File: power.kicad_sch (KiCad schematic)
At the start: 0 parts

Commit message: moved over a lot of schematic from the bitaxe
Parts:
- added C10: 180pF, Capacitor_SMD:C_0805_2012Metric, symbol Device:C
- added C11: 1.5nF, Capacitor_SMD:C_0805_2012Metric, symbol Device:C
- added C12: 0.1uF, Capacitor_SMD:C_0402_1005Metric, symbol Device:C
- added C13: 10uF, Capacitor_SMD:C_0805_2012Metric, symbol Device:C
- added C14: 470pF, Capacitor_SMD:C_0805_2012Metric, symbol Device:C
- added C15: 220uF, TPS40305_supply:CAP_2R5TPE220MAFB, symbol Device:C_Polarized
- added C16: 100uF, Capacitor_SMD:C_1206_3216Metric, symbol Device:C
- added C17: 1uF, Capacitor_SMD:C_0402_1005Metric, symbol Device:C
- added C5, C6, C7: 47uF, Capacitor_SMD:C_1210_3225Metric, symbol Device:C
- added C8: 1uF, Capacitor_SMD:C_0805_2012Metric, symbol Device:C
- added C9: 3.3nF, Capacitor_SMD:C_0402_1005Metric, symbol Device:C
- added L1: 150nH, TPS40305_supply:FP1005R1-R15-R, symbol Device:L
- added Q1, Q2: CSD17311Q5, TPS40305_supply:CSD17311Q5, symbol TPS40305:Q_NMOS_CSD17311Q5
- added R10: 3.32k, Resistor_SMD:R_0402_1005Metric, symbol Device:R_US
- added R11: 80k, Resistor_SMD:R_0402_1005Metric, symbol Device:R_US
- added R12: DNP, Resistor_SMD:R_0402_1005Metric, symbol Device:R_US
- added R5: 3.83k, Resistor_SMD:R_0402_1005Metric, symbol Device:R_US
- added R6: 100k, Resistor_SMD:R_0402_1005Metric, symbol Device:R_US
- added R7: 4.12k, Resistor_SMD:R_0402_1005Metric, symbol Device:R_US
- added R8: 1.33k, Resistor_SMD:R_0402_1005Metric, symbol Device:R_US
- added R9: 4.99k, Resistor_SMD:R_0402_1005Metric, symbol Device:R_US
- added U2: TPS40305, TPS40305_supply:TPS40305, symbol TPS40305:TPS40305
- added U3: DS4432U+, Package_SO:TSSOP-8_3x3mm_P0.65mm, symbol TPS40305:DS4432U+
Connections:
- new net: Q1.4 (G), U2.7 (HDRV)
- new net: C13.1, R6.2, U2.10 (BP)
- new net: C11.2, R5.1
- new net: C14.1, R8.2
- new net: C10.1, C11.1, U2.4 (COMP)
- new net: Q2.4 (G), R7.1, U2.9 (LDRV)
- new net: C12.1, U2.6 (BOOT)
- new net: R12.1, U3.3 (FS1)
- new net: R11.1, U3.5 (FS0)
- new net: C9.1, U2.2 (SS)
- new net 3V3: C17.1, U3.8 (VCC)
- new net 5V: C5.1, C6.1, C7.1, C8.1, Q1.5 (D), U2.1 (VDD)
- new net GND: C13.2, C15.2, C16.2, C17.2, C5.2, C6.2, C7.2, C8.2, C9.2, Q2.1, Q2.2, Q2.3 (S), R10.2, R11.2, R12.2, R7.2, U2.11 (GND), U3.4 (GND)
- new net OUT0: C10.2, C14.2, R10.1, R5.2, R9.2, U2.5 (FB), U3.6 (OUT0)
- new net OUT1: U3.7 (OUT1)
- new net PGOOD: R6.1, U2.3 (PGOOD)
- new net SCL: U3.2 (SCL)
- new net SDA: U3.1 (SDA)
- new net SW: C12.2, L1.1, Q1.1, Q1.2, Q1.3 (S), Q2.5 (D), U2.8 (SW)
- new net VOUT: C15.1, C16.1, L1.2, R8.1, R9.1
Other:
- note added: "I2C Address: 0x48"
- note added: "Vfb = 0.6V"

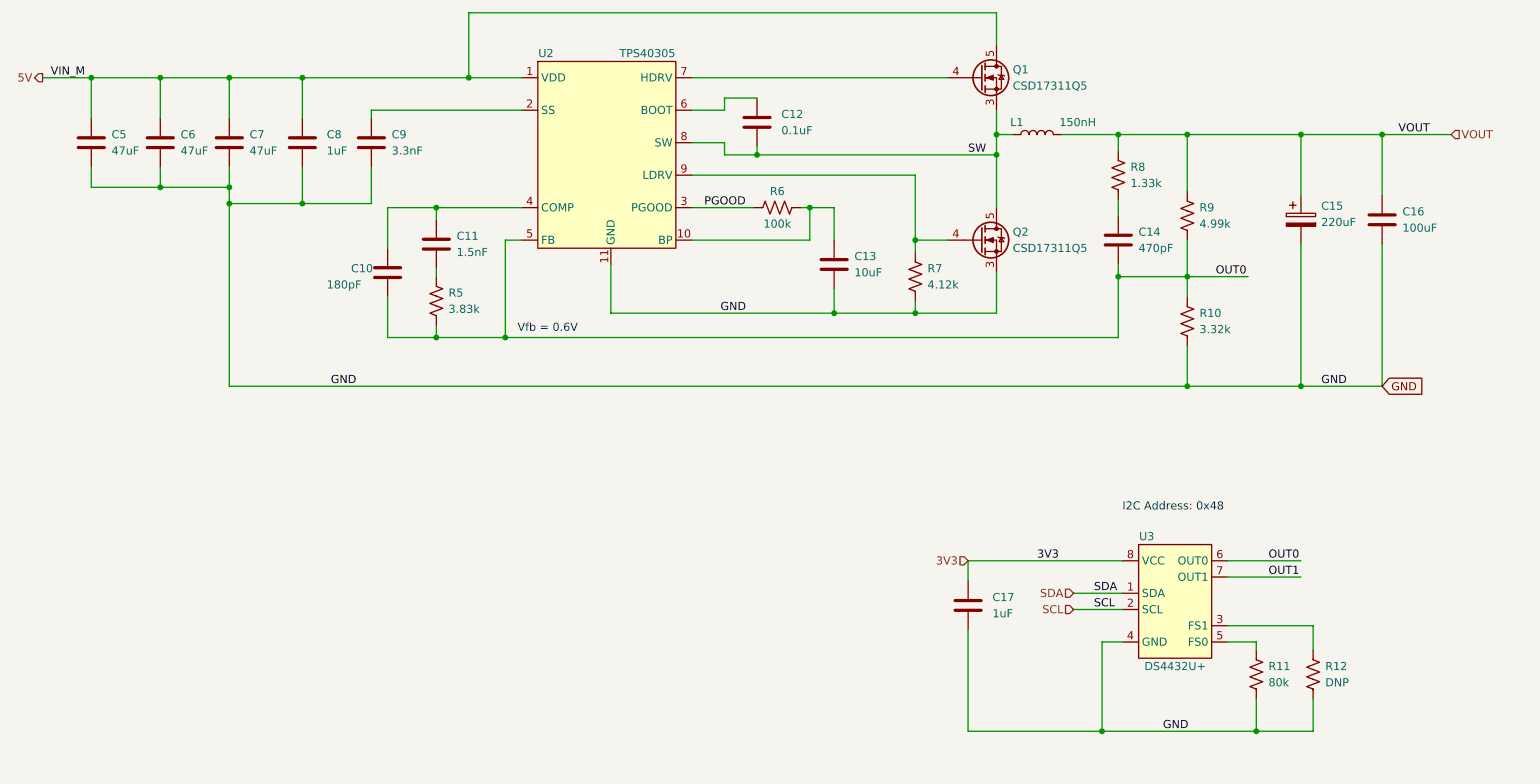
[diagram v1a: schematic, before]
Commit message: cleared up some part reference designator madness
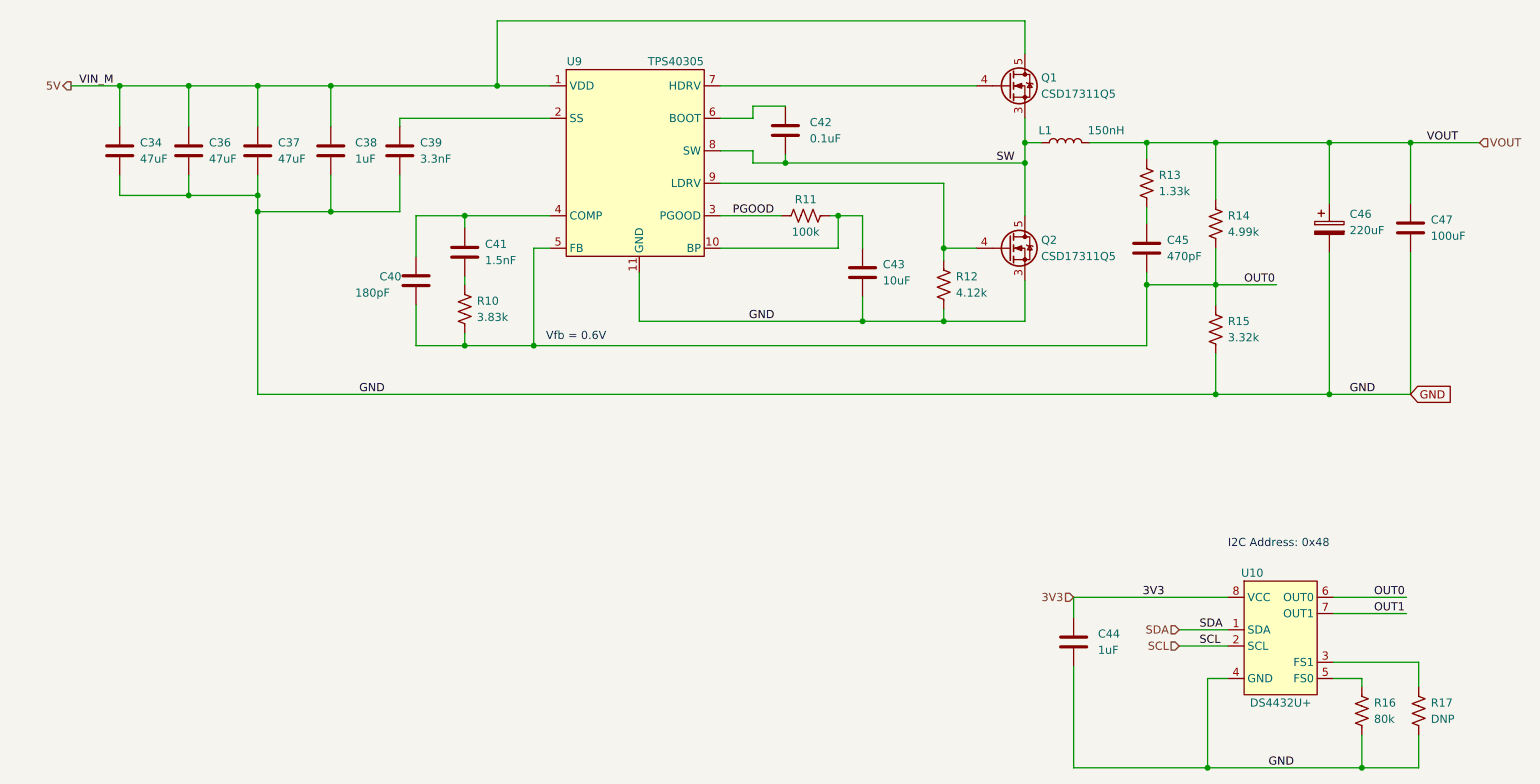
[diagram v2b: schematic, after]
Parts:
- removed C10: 180pF, Capacitor_SMD:C_0805_2012Metric, symbol Device:C
- removed C11: 1.5nF, Capacitor_SMD:C_0805_2012Metric, symbol Device:C
- removed C12: 0.1uF, Capacitor_SMD:C_0402_1005Metric, symbol Device:C
- removed C13: 10uF, Capacitor_SMD:C_0805_2012Metric, symbol Device:C
- removed C14: 470pF, Capacitor_SMD:C_0805_2012Metric, symbol Device:C
- removed C15: 220uF, TPS40305_supply:CAP_2R5TPE220MAFB, symbol Device:C_Polarized
- removed C16: 100uF, Capacitor_SMD:C_1206_3216Metric, symbol Device:C
- removed C17: 1uF, Capacitor_SMD:C_0402_1005Metric, symbol Device:C
- removed C5, C6, C7: 47uF, Capacitor_SMD:C_1210_3225Metric, symbol Device:C
- removed C8: 1uF, Capacitor_SMD:C_0805_2012Metric, symbol Device:C
- removed C9: 3.3nF, Capacitor_SMD:C_0402_1005Metric, symbol Device:C
- removed R5: 3.83k, Resistor_SMD:R_0402_1005Metric, symbol Device:R_US
- removed R6: 100k, Resistor_SMD:R_0402_1005Metric, symbol Device:R_US
- removed R7: 4.12k, Resistor_SMD:R_0402_1005Metric, symbol Device:R_US
- removed R8: 1.33k, Resistor_SMD:R_0402_1005Metric, symbol Device:R_US
- removed R9: 4.99k, Resistor_SMD:R_0402_1005Metric, symbol Device:R_US
- removed U2: TPS40305, TPS40305_supply:TPS40305, symbol TPS40305:TPS40305
- removed U3: DS4432U+, Package_SO:TSSOP-8_3x3mm_P0.65mm, symbol TPS40305:DS4432U+
- added C34, C36, C37: 47uF, Capacitor_SMD:C_1210_3225Metric, symbol Device:C
- added C38: 1uF, Capacitor_SMD:C_0805_2012Metric, symbol Device:C
- added C39: 3.3nF, Capacitor_SMD:C_0402_1005Metric, symbol Device:C
- added C40: 180pF, Capacitor_SMD:C_0805_2012Metric, symbol Device:C
- added C41: 1.5nF, Capacitor_SMD:C_0805_2012Metric, symbol Device:C
- added C42: 0.1uF, Capacitor_SMD:C_0402_1005Metric, symbol Device:C
- added C43: 10uF, Capacitor_SMD:C_0805_2012Metric, symbol Device:C
- added C44: 1uF, Capacitor_SMD:C_0402_1005Metric, symbol Device:C
- added C45: 470pF, Capacitor_SMD:C_0805_2012Metric, symbol Device:C
- added C46: 220uF, TPS40305_supply:CAP_2R5TPE220MAFB, symbol Device:C_Polarized
- added C47: 100uF, Capacitor_SMD:C_1206_3216Metric, symbol Device:C
- added R13: 1.33k, Resistor_SMD:R_0402_1005Metric, symbol Device:R_US
- added R14: 4.99k, Resistor_SMD:R_0402_1005Metric, symbol Device:R_US
- added R15: 3.32k, Resistor_SMD:R_0402_1005Metric, symbol Device:R_US
- added R16: 80k, Resistor_SMD:R_0402_1005Metric, symbol Device:R_US
- added R17: DNP, Resistor_SMD:R_0402_1005Metric, symbol Device:R_US
- added U10: DS4432U+, Package_SO:TSSOP-8_3x3mm_P0.65mm, symbol TPS40305:DS4432U+
- added U9: TPS40305, TPS40305_supply:TPS40305, symbol TPS40305:TPS40305
- R10: value 3.32k -> 3.83k; DK 311-3.32KLRCT-ND -> 311-3.83KLRCT-ND; PARTNO RC0402FR-073K32L -> RC0402FR-073K83L
- R11: value 80k -> 100k; DK 311-80.6KLRCT-ND -> 311-100KJRCT-ND; PARTNO RC0402FR-0780K6L -> RC0402JR-07100KL
- R12: value DNP -> 4.12k; DK (none) -> RMCF0402FT4K12CT-ND; DNP T -> (none); PARTNO (none) -> RMCF0402FT4K12
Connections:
- net 3V3: now also C44.1, U10.8 (VCC)
- net 5V: now also C34.1, C36.1, C37.1, C38.1, U9.1 (VDD)
- net GND: now also C34.2, C36.2, C37.2, C38.2, C39.2, C43.2, C44.2, C46.2, C47.2, R15.2, R16.2, R17.2, U10.4 (GND), U9.11 (GND); no longer R10.2, R11.2
- net OUT0: now also R10.2, C40.2, C45.2, R14.2, R15.1, U10.6 (OUT0), U9.5 (FB); no longer R10.1
- net OUT1: now also U10.7 (OUT1)
- net PGOOD: now also R11.1, U9.3 (PGOOD)
- net SCL: now also U10.2 (SCL)
- net SDA: now also U10.1 (SDA)
- net SW: now also C42.2, U9.8 (SW)
- net VOUT: now also C46.1, C47.1, R13.1, R14.1
- net at Q1.4 (G): now also U9.7 (HDRV)
- net at Q2.4 (G): now also R12.1, U9.9 (LDRV)
- new net: C39.1, U9.2 (SS)
- new net: C40.1, C41.1, U9.4 (COMP)
- new net: C43.1, R11.2, U9.10 (BP)
- new net: C41.2, R10.1
- new net: R17.1, U10.3 (FS1)
- new net: C45.1, R13.2
- new net: R16.1, U10.5 (FS0)
- new net: C42.1, U9.6 (BOOT)

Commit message: cleanup. added LCSC fan connector
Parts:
- added DC1: DC-044K-D025, lcsc:DC-IN-TH_DC-044K-D025, symbol lcsc:DC-044K-D025
- L1: LCSC Part (none) -> C2453377
- Q1, Q2: LCSC Part (none) -> C139640
- U10: LCSC Part (none) -> C2679620
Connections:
- net 5V: now also DC1.4
- net GND: now also DC1.1, DC1.2, DC1.3, DC1.6
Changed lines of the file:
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@@
   (junction (at 235.585 81.28) (diameter 0) (color 0 0 0 0)
   )
+  (junction (at 54.61 114.3) (diameter 0) (color 0 0 0 0)
+  )
   (junction (at 187.96 45.085) (diameter 0) (color 0 0 0 0)
   )
@@
   (junction (at 217.805 64.135) (diameter 0) (color 0 0 0 0)
   )
+  (junction (at 195.58 113.03) (diameter 0) (color 0 0 0 0)
+  )
   (junction (at 105.41 33.02) (diameter 0) (color 0 0 0 0)
   )
@@
   (junction (at 162.56 69.85) (diameter 0) (color 0 0 0 0)
   )
+  (junction (at 54.61 116.84) (diameter 0) (color 0 0 0 0)
+  )
   (junction (at 79.375 33.02) (diameter 0) (color 0 0 0 0)
   )
@@
     (stroke (width 0) (type default))
   )
+  (wire (pts (xy 52.07 111.76) (xy 71.755 111.76))
+    (stroke (width 0) (type default))
+  )
   (wire (pts (xy 67.945 52.705) (xy 67.945 81.28))
     (stroke (width 0) (type default))
@@
     (stroke (width 0) (type default))
   )
+  (wire (pts (xy 54.61 116.84) (xy 54.61 114.3))
+    (stroke (width 0) (type default))
+  )
   (wire (pts (xy 145.415 45.085) (xy 150.495 45.085))
     (stroke (width 0) (type default))
@@
     (stroke (width 0) (type default))
   )
+  (wire (pts (xy 52.07 114.3) (xy 54.61 114.3))
+    (stroke (width 0) (type default))
+  )
   (wire (pts (xy 113.665 53.34) (xy 100.33 53.34))
     (stroke (width 0) (type default))
@@
     (stroke (width 0) (type default))
   )
+  (wire (pts (xy 52.07 109.22) (xy 57.15 109.22))
+    (stroke (width 0) (type default))
+  )
   (wire (pts (xy 145.415 38.1) (xy 145.415 36.195))
     (stroke (width 0) (type default))
@@
     (stroke (width 0) (type default))
   )
+  (wire (pts (xy 52.07 119.38) (xy 54.61 119.38))
+    (stroke (width 0) (type default))
+  )
   (wire (pts (xy 217.805 74.93) (xy 217.805 81.28))
     (stroke (width 0) (type default))
@@
     (stroke (width 0) (type default))
   )
+  (wire (pts (xy 54.61 119.38) (xy 54.61 116.84))
+    (stroke (width 0) (type default))
+  )
   (wire (pts (xy 100.33 53.34) (xy 92.71 53.34))
     (stroke (width 0) (type default))
@@
     (stroke (width 0) (type default))
   )
+  (wire (pts (xy 191.135 113.03) (xy 195.58 113.03))
+    (stroke (width 0) (type default))
+  )
   (wire (pts (xy 162.56 66.04) (xy 162.56 69.85))
     (stroke (width 0) (type default))
@@
     (stroke (width 0) (type default))
   )
+  (wire (pts (xy 52.07 116.84) (xy 54.61 116.84))
+    (stroke (width 0) (type default))
+  )
   (wire (pts (xy 195.58 123.825) (xy 195.58 139.7))
     (stroke (width 0) (type default))
@@
     (stroke (width 0) (type default))
   )
+  (wire (pts (xy 54.61 114.3) (xy 57.15 114.3))
+    (stroke (width 0) (type default))
+  )
   (wire (pts (xy 207.01 52.07) (xy 207.01 54.61))
     (stroke (width 0) (type default))
@@
     (effects (font (size 1.27 1.27)) (justify left bottom))
   )
-  (label "VIN_M" (at 40.005 33.02 0) (fields_autoplaced)
+  (label "VIN" (at 40.005 33.02 0) (fields_autoplaced)
     (effects (font (size 1.27 1.27)) (justify left bottom))
   )
@@
     (effects (font (size 1.27 1.27)) (justify left bottom))
   )
+  (label "VIN" (at 64.77 111.76 0) (fields_autoplaced)
+    (effects (font (size 1.27 1.27)) (justify left bottom))
+  )
   (label "GND" (at 83.82 81.28 0) (fields_autoplaced)
     (effects (font (size 1.27 1.27)) (justify left bottom))
@@
   )
   (label "3V3" (at 206.375 113.03 0) (fields_autoplaced)
+    (effects (font (size 1.27 1.27)) (justify left bottom))
+  )
+  (label "GND" (at 52.705 109.22 0) (fields_autoplaced)
+    (effects (font (size 1.27 1.27)) (justify left bottom))
+  )
+  (label "GND" (at 52.705 114.3 0) (fields_autoplaced)
     (effects (font (size 1.27 1.27)) (justify left bottom))
   )
@@
     (effects (font (size 1.27 1.27)) (justify right))
   )
-  (hierarchical_label "3V3" (shape input) (at 195.58 113.03 180) (fields_autoplaced)
+  (hierarchical_label "3V3" (shape input) (at 191.135 113.03 180) (fields_autoplaced)
     (effects (font (size 1.27 1.27)) (justify right))
   )
@@
     )
     (property "PARTNO" "CSD17311Q5" (at 185.42 33.02 0)
+      (effects (font (size 1.27 1.27)) hide)
+    )
+    (property "LCSC Part" "C139640" (at 185.42 33.02 0)
       (effects (font (size 1.27 1.27)) hide)
     )
@@
       (effects (font (size 1.27 1.27)) hide)
     )
+    (property "LCSC Part" "C139640" (at 185.42 58.42 0)
+      (effects (font (size 1.27 1.27)) hide)
+    )
     (pin "1")
     (pin "2")
@@
     )
     (property "PARTNO" "DS4432U+" (at 228.6 119.38 0)
+      (effects (font (size 1.27 1.27)) hide)
+    )
+    (property "LCSC Part" "C2679620" (at 228.6 119.38 0)
       (effects (font (size 1.27 1.27)) hide)
     )
@@
       (effects (font (size 1.27 1.27)) hide)
     )
+    (property "LCSC Part" "C2453377" (at 194.31 41.91 90)
+      (effects (font (size 1.27 1.27)) hide)
+    )
     (pin "1")
     (pin "2")
@@
         )
       )
+    )
+  )
+  (symbol (lib_id "lcsc:DC-044K-D025") (at 44.45 114.3 0) (unit 1)
+    (in_bom yes) (on_board yes) (dnp no)
+    (property "Reference" "DC1" (at 38.1 107.95 0)
+      (effects (font (size 1.27 1.27)))
+    )
+    (property "Value" "DC-044K-D025" (at 34.29 120.65 0)
+      (effects (font (size 1.27 1.27)))
+    )
+    (property "Footprint" "lcsc:DC-IN-TH_DC-044K-D025" (at 44.45 127 0)
+      (effects (font (size 1.27 1.27)) hide)
+    )
+    (property "Datasheet" "" (at 44.45 114.3 0)
+      (effects (font (size 1.27 1.27)) hide)
+    )
+    (property "Manufacturer" "G-Switch" (at 44.45 129.54 0)
+      (effects (font (size 1.27 1.27)) hide)
+    )
+    (property "LCSC Part" "C963204" (at 44.45 132.08 0)
+      (effects (font (size 1.27 1.27)) hide)
+    )
+    (property "JLC Part" "Extended Part" (at 44.45 134.62 0)
+      (effects (font (size 1.27 1.27)) hide)
+    )
+    (pin "1")
+    (pin "2")
+    (pin "3")
+    (pin "4")
+    (pin "6")
+    (instances
+      (project "Hashat"
+        (path "/00740941-7ad8-466a-a267-188591e2b5c4"
+          (reference "DC1") (unit 1)
+        )
+        (path "/00740941-7ad8-466a-a267-188591e2b5c4/a06b4d76-7549-4f87-b16c-eb4e8ad457b9"
+          (reference "DC1") (unit 1)
+        )
+      )
